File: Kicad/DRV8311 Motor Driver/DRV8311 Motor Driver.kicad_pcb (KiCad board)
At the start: 4 copper layers, 15 x 15 mm, 29 parts, among them J1 1.27mm pin header, J10 Keystone 3569, J11 Keystone 3579, J2 1.27mm pin header, J3 Keystone 3579, J4 Molex Picoblade, J5 Keystone 3569, J6 Keystone 3569, J7 Keystone 3579, J8 Keystone 3569, J9 Keystone 3579, U1 DRV8311HRRWR

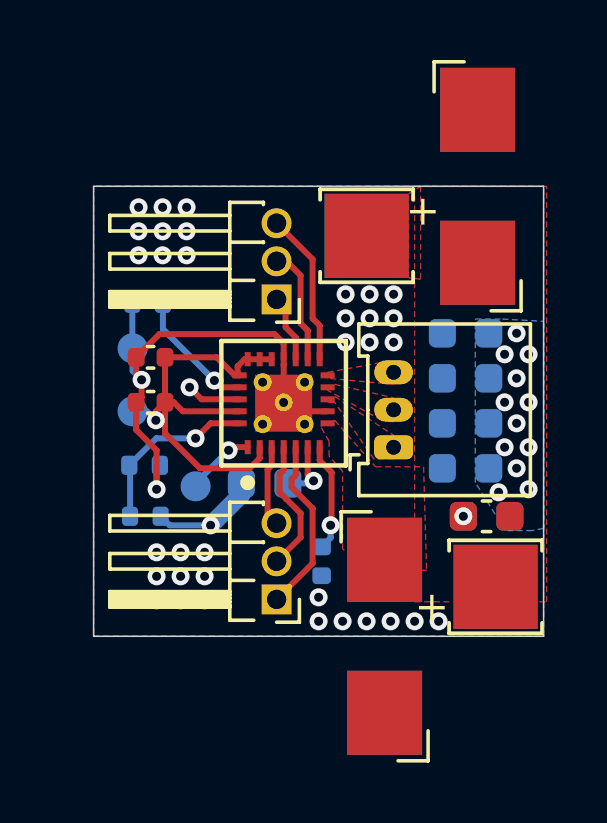
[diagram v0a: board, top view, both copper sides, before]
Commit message: Updated 3D models and exported 3D model for DRV8311 board
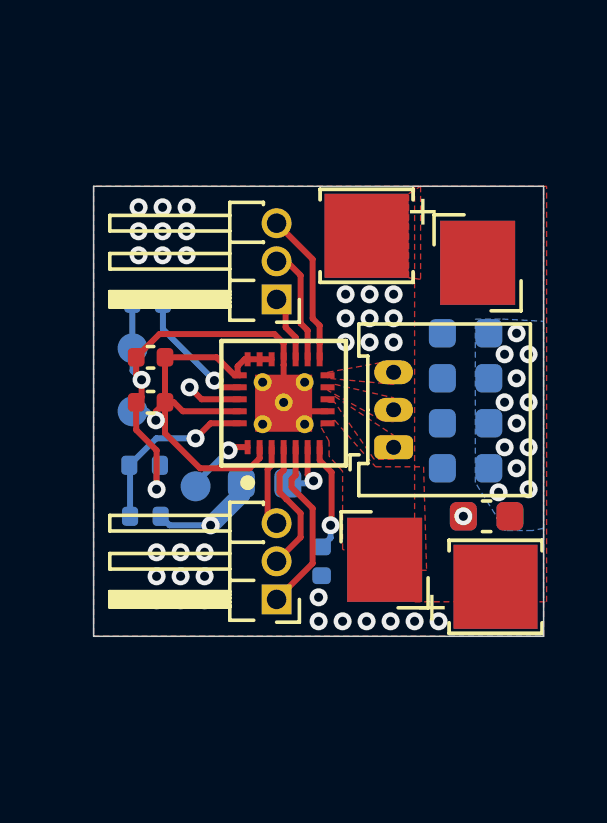
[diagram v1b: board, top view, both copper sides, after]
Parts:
- J10, J5, J6, J8: footprint custom_Connector:Keystone_3569 -> custom_Connector:Keystone_3569_half
- turned J5 to 0 degrees
- turned J6 to 180 degrees

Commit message: Fixed headers and connectors miss-alignments
Almost everything was misaligned. The holes on the hub to hub headers must be 2.9mm from the edge, the header holes on the motor drivers must be 4.5mm from the edge, and the centers of the power connectors(either gender) must be 2.15mm from the edge
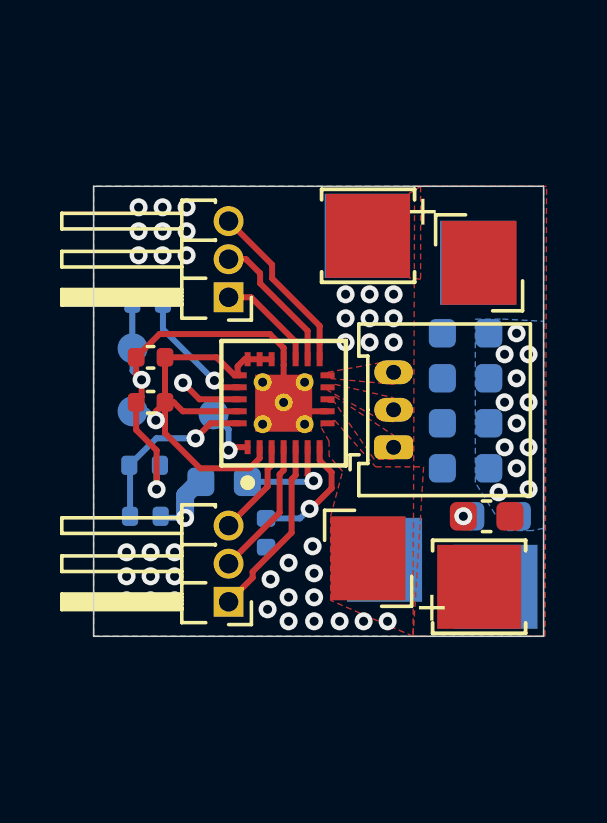
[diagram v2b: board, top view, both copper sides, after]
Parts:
- moved TP3 2.47 mm to (167.8, 101.8)
- moved C3 2.08 mm to (169.6, 105.8)
- moved J1 1.60 mm to (168.3, 108.0)
- moved J2 1.60 mm to (168.3, 97.9)
- moved C2 1.35 mm to (168.2, 104.0)
- moved J6 0.55 mm to (172.9, 109.2)
- moved J7 0.55 mm to (176.7, 107.5)
- moved C10 0.25 mm to (177.2, 105.2)
- moved J9 0.05 mm to (172.9, 95.8)
- moved J8 0.05 mm to (176.7, 94.2)
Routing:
- net Net-(U1-CP): track 2.10 -> 3.43 mm
- net Net-(J2-Pin_1): track 2.26 -> 3.43 mm
- net Net-(J2-Pin_2): track 3.89 -> 4.77 mm
- net VDD: track 7.30 -> 6.49 mm
- net Net-(J2-Pin_3): track 5.13 -> 5.86 mm
- net GNDPWR: vias 35 -> 40

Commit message: Fixed 0.2mm offset in 3d model of Keystone 3579 connector
It was inset into the pcb a little which was causing some vertical misalignment in the CAD model. This affects nothing in real life, just a nice quality of life thing.
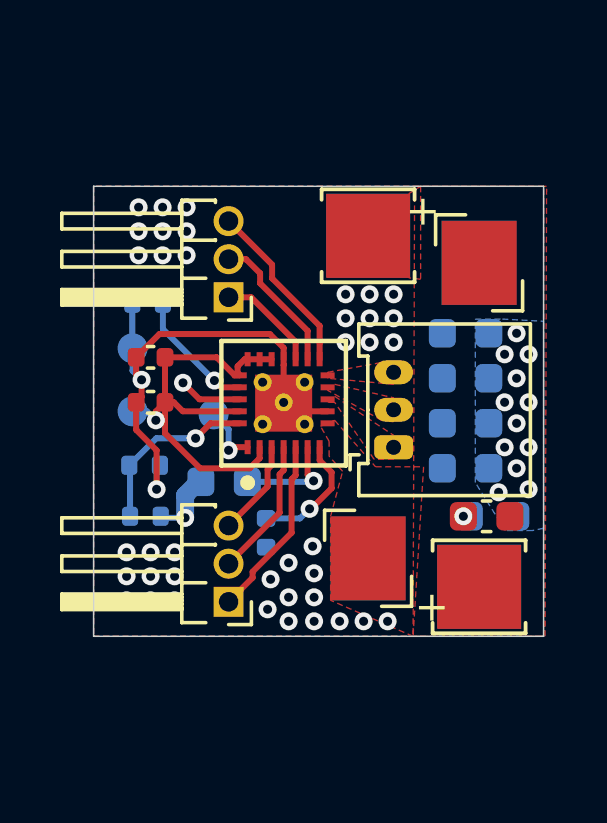
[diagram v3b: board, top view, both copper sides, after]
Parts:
- moved J5 0.55 mm to (172.9, 109.2)
- moved J3 0.55 mm to (176.7, 107.5)
- moved C10 0.05 mm to (177.1, 105.2)
- moved J10 0.05 mm to (176.7, 94.2)
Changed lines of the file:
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@@
 		(model "${KICAD_USER_CUSTOM}/custom_Connector.pretty/Keystone 3579.step"
 			(offset
-				(xyz 0 0 0)
+				(xyz 0 0 0.2)
 			)
 			(scale
@@
 		(model "${KICAD_USER_CUSTOM}/custom_Connector.pretty/Keystone 3579.step"
 			(offset
-				(xyz 0 0 0)
+				(xyz 0 0 0.2)
 			)
 			(scale
@@
 	(footprint "custom_Connector:Keystone_3569_half"
 		(layer "B.Cu")
-		(at 176.6 94.2 180)
+		(at 176.65 94.2 180)
 		(descr "Fuse Clip 15 A 500V 1 Circuit Blade Surface Mount. Also goes with Keystone 3579 board edge conn")
 		(tags "Fuse")
@@
 	(footprint "custom_Connector:Keystone_3569_half"
 		(layer "B.Cu")
-		(at 173.5 109.2)
+		(at 172.95 109.15)
 		(descr "Fuse Clip 15 A 500V 1 Circuit Blade Surface Mount. Also goes with Keystone 3579 board edge conn")
 		(tags "Fuse")
@@
 	(footprint "Capacitor_SMD:C_0603_1608Metric"
 		(layer "B.Cu")
-		(at 177.15 105.2 180)
+		(at 177.1 105.2 180)
 		(descr "Capacitor SMD 0603 (1608 Metric), square (rectangular) end terminal, IPC_7351 nominal, (Body size source: IPC-SM-782 page 76, https://www.pcb-3d.com/wordpress/wp-content/uploads/ipc-sm-782a_amendment_1_and_2.pdf), generated with kicad-footprint-generator")
 		(tags "capacitor")
@@
 	(footprint "custom_Connector:Keystone_3579"
 		(layer "B.Cu")
-		(at 177.2 107.55 180)
+		(at 176.65 107.55 180)
 		(property "Reference" "J3"
 			(at 0.882 3.3964 0)
@@
 		(model "${KICAD_USER_CUSTOM}/custom_Connector.pretty/Keystone 3579.step"
 			(offset
-				(xyz 0 0 0)
+				(xyz 0 0 0.2)
 			)
 			(scale
@@
 	(footprint "custom_Connector:Keystone_3579"
 		(layer "B.Cu")
-		(at 172.900001 95.85)
+		(at 172.95 95.85)
 		(property "Reference" "J11"
 			(at 0.882 3.3964 0)
@@
 		(model "${KICAD_USER_CUSTOM}/custom_Connector.pretty/Keystone 3579.step"
 			(offset
-				(xyz 0 0 0)
+				(xyz 0 0 0.2)
 			)
 			(scale

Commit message: Added LCSC part numbers, DNP attr, and exported Gerbers
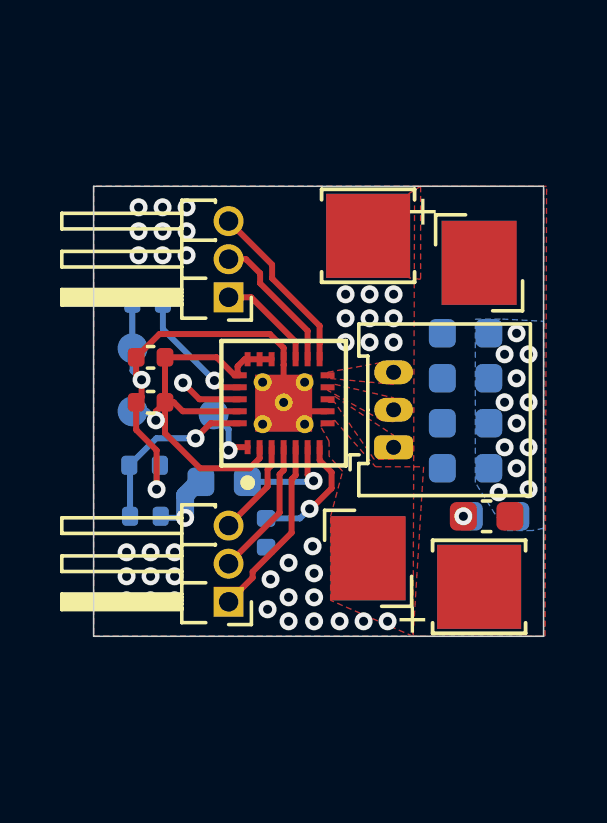
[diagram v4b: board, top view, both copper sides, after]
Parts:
- C2, C3, C6, C7: value 0.1uF, 16v -> 100nF, 16v
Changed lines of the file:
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@@
 			)
 		)
+		(property "LCSC" "C505275"
+			(at 0 0 0)
+			(layer "F.SilkS")
+			(hide yes)
+			(effects
+				(font
+					(size 1.27 1.27)
+					(thickness 0.15)
+				)
+			)
+		)
 		(property ki_fp_filters "Connector*:*_1x??_*")
 		(sheetname "Root")
@@
 			)
 		)
+		(property "LCSC" "C23733"
+			(at 0 0 0)
+			(layer "F.SilkS")
+			(hide yes)
+			(effects
+				(font
+					(size 1.27 1.27)
+					(thickness 0.15)
+				)
+			)
+		)
 		(property ki_fp_filters "C_*")
 		(sheetname "Root")
@@
 			)
 		)
+		(property "LCSC" "C5218862"
+			(at 0 0 0)
+			(layer "F.SilkS")
+			(hide yes)
+			(effects
+				(font
+					(size 1.27 1.27)
+					(thickness 0.15)
+				)
+			)
+		)
 		(property ki_fp_filters "RRW0024-MFG")
 		(sheetname "Root")
@@
 			)
 		)
-		(property "Value" "0.1uF, 16v"
+		(property "Value" "100nF, 16v"
 			(at 0 1.43 0)
 			(layer "F.Fab")
@@
 			)
 		)
+		(property "LCSC" "C14663"
+			(at 0 0 0)
+			(layer "F.SilkS")
+			(hide yes)
+			(effects
+				(font
+					(size 1.27 1.27)
+					(thickness 0.15)
+				)
+			)
+		)
 		(property ki_fp_filters "C_*")
 		(sheetname "Root")
@@
 		(sheetname "Root")
 		(sheetfile "DRV8311 Motor Driver.kicad_sch")
-		(attr through_hole)
+		(attr through_hole dnp)
 		(fp_line
 			(start 5.56 2.8)
@@
 			)
 		)
-		(property "Value" "0.1uF, 16v"
+		(property "Value" "100nF, 16v"
 			(at 0 1.16 0)
 			(layer "F.Fab")
@@
 			)
 		)
+		(property "LCSC" "C1525"
+			(at 0 0 0)
+			(layer "F.SilkS")
+			(hide yes)
+			(effects
+				(font
+					(size 1.27 1.27)
+					(thickness 0.15)
+				)
+			)
+		)
 		(property ki_fp_filters "C_*")
 		(sheetname "Root")
@@
 		(sheetname "Root")
 		(sheetfile "DRV8311 Motor Driver.kicad_sch")
-		(attr through_hole)
+		(attr through_hole dnp)
 		(fp_line
 			(start 5.56 2.8)
@@
 			)
 		)
+		(property "LCSC" "C25774"
+			(at 0 0 0)
+			(layer "B.SilkS")
+			(hide yes)
+			(effects
+				(font
+					(size 1.27 1.27)
+					(thickness 0.15)
+				)
+			)
+		)
 		(property ki_fp_filters "R_*")
 		(sheetname "Root")
@@
 			)
 		)
+		(property "LCSC" "C96446"
+			(at 0 0 0)
+			(layer "B.SilkS")
+			(hide yes)
+			(effects
+				(font
+					(size 1.27 1.27)
+					(thickness 0.15)
+				)
+			)
+		)
 		(property ki_fp_filters "C_*")
 		(sheetname "Root")
@@
 			)
 		)
+		(property "LCSC" "C96446"
+			(at 0 0 0)
+			(layer "B.SilkS")
+			(hide yes)
+			(effects
+				(font
+					(size 1.27 1.27)
+					(thickness 0.15)
+				)
+			)
+		)
 		(property ki_fp_filters "C_*")
 		(sheetname "Root")
@@
 			)
 		)
-		(property "Value" "0.1uF, 16v"
+		(property "Value" "100nF, 16v"
 			(at 0 -1.16 90)
 			(layer "B.Fab")
@@
 			)
 		)
+		(property "LCSC" "C1525"
+			(at 0 0 0)
+			(layer "B.SilkS")
+			(hide yes)
+			(effects
+				(font
+					(size 1.27 1.27)
+					(thickness 0.15)
+				)
+			)
+		)
 		(property ki_fp_filters "C_*")
 		(sheetname "Root")
@@
 			)
 		)
+		(property "LCSC" "C96446"
+			(at 0 0 0)
+			(layer "B.SilkS")
+			(hide yes)
+			(effects
+				(font
+					(size 1.27 1.27)
+					(thickness 0.15)
+				)
+			)
+		)
 		(property ki_fp_filters "C_*")
 		(sheetname "Root")
@@
 			)
 		)
+		(property "LCSC" "C96446"
+			(at 0 0 0)
+			(layer "B.SilkS")
+			(hide yes)
+			(effects
+				(font
+					(size 1.27 1.27)
+					(thickness 0.15)
+				)
+			)
+		)
 		(property ki_fp_filters "C_*")
 		(sheetname "Root")
@@
 			)
 		)
+		(property "LCSC" "C25792"
+			(at 0 0 0)
+			(layer "B.SilkS")
+			(hide yes)
+			(effects
+				(font
+					(size 1.27 1.27)
+					(thickness 0.15)
+				)
+			)
+		)
 		(property ki_fp_filters "R_*")
 		(sheetname "Root")
@@
 			)
 		)
-		(property "Value" "0.1uF, 16v"
+		(property "Value" "100nF, 16v"
 			(at 0 -1.43 0)
 			(layer "B.Fab")
@@
 			)
 		)
+		(property "LCSC" "C14663"
+			(at 0 0 0)
+			(layer "B.SilkS")
+			(hide yes)
+			(effects
+				(font
+					(size 1.27 1.27)
+					(thickness 0.15)
+				)
+			)
+		)
 		(property ki_fp_filters "C_*")
 		(sheetname "Root")
@@
 			)
 		)
+		(property "LCSC" "C96446"
+			(at 0 0 0)
+			(layer "B.SilkS")
+			(hide yes)
+			(effects
+				(font
+					(size 1.27 1.27)
+					(thickness 0.15)
+				)
+			)
+		)
 		(property ki_fp_filters "C_*")
 		(sheetname "Root")
@@
 			)
 		)
+		(property "LCSC" "C25741"
+			(at 0 0 0)
+			(layer "B.SilkS")
+			(hide yes)
+			(effects
+				(font
+					(size 1.27 1.27)
+					(thickness 0.15)
+				)
+			)
+		)
 		(property ki_fp_filters "R_*")
 		(sheetname "Root")
@@
 	)
 	(gr_text "-"
-		(at 175.649999 109.1 -0)
+		(at 175.1 109.1 -0)
 		(layer "B.SilkS")
 		(effects
@@
 	)
 	(gr_text "+"
-		(at 174.5 108.8 -0)
+		(at 173.85 109.2 -0)
 		(layer "F.SilkS")
 		(effects
